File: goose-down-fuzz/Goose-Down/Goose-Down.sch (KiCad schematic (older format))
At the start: 45 parts, among them J1 In, J2 Out, J3 PWR, J4 GND, J5 SW, J6 GND, Q1 BC104, Q2 BC104, Q3 2n5458, Q4 2n5088, U1 LM741, U2 LM741

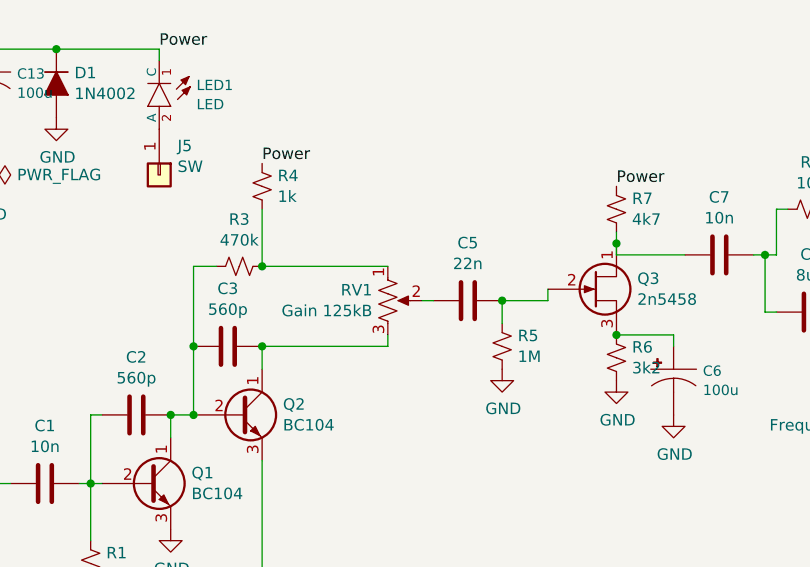
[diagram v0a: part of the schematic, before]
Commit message: Update GD with Var-resistor Gain wiring, add Tone Stack to LTSpice plot
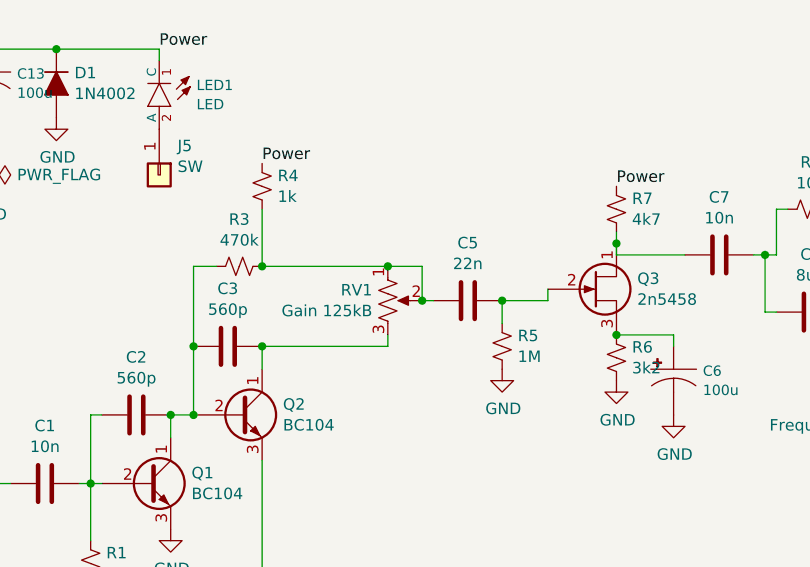
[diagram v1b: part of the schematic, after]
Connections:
- net at R3.1, R4.2, RV1.1: now also C5.2, RV1.2
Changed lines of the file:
@@
 $EndComp
 Connection ~ 2050 2600
+Wire Wire Line
+	3950 3100 4100 3100
+Wire Wire Line
+	4100 3100 4100 3250
+Connection ~ 3950 3100
+Connection ~ 4100 3250
 $EndSCHEMATC
